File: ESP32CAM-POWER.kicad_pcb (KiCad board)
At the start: 2 copper layers, 80 x 80 mm, 33 parts, among them J1 Screw_Terminal_01x02, J2 Conn_01x03_Male, SW1 TS-1187A-B-A-B, U1 DC-DC-BOARD, U2 ESP32-CAM

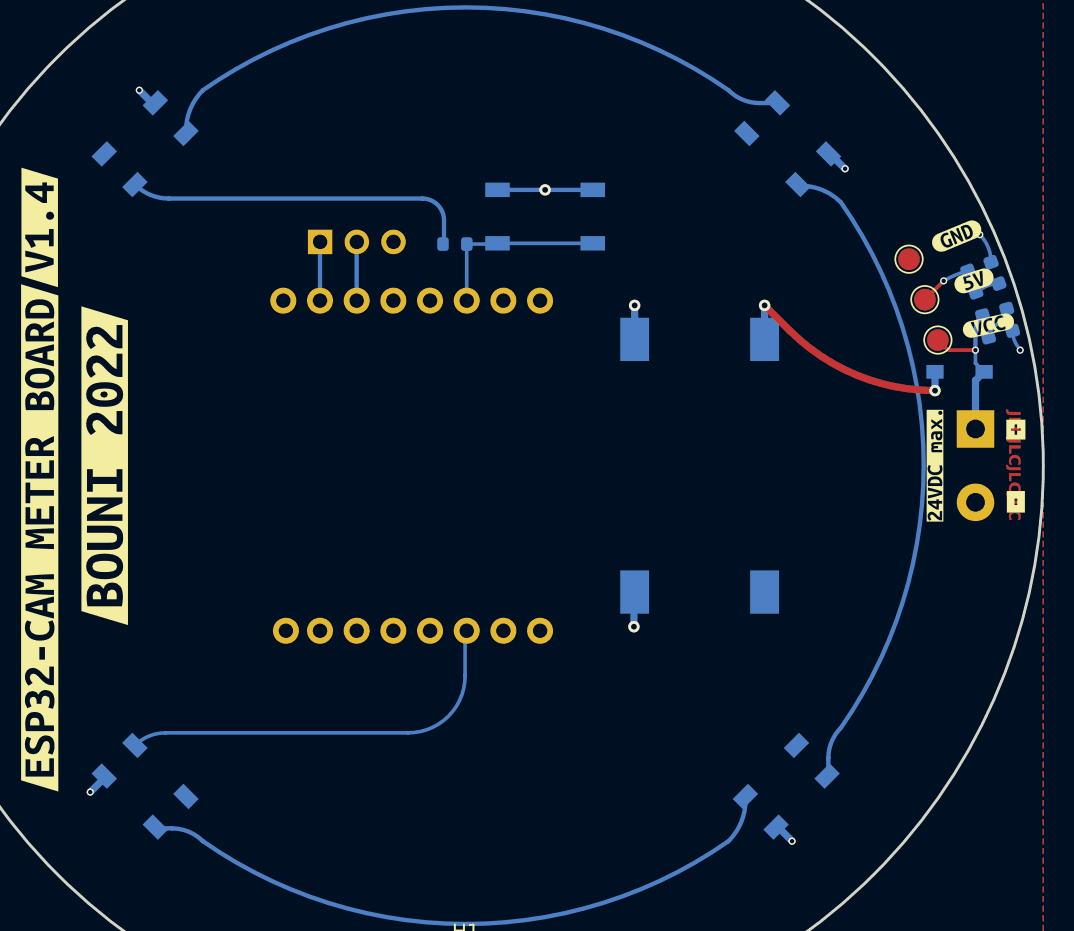
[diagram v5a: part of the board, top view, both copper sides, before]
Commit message: fixed several bugs, replaced DCDC Module with onboard step down
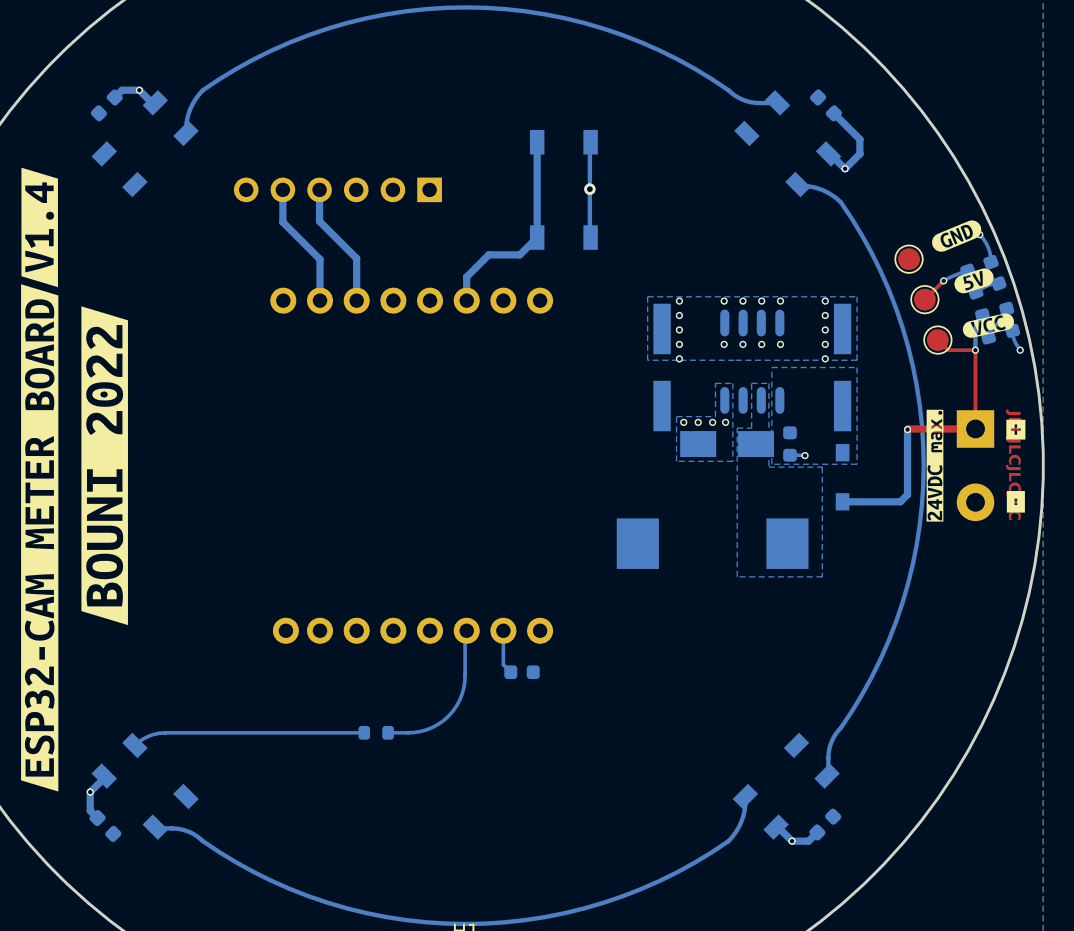
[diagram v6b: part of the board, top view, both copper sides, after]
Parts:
- removed U1: DC-DC-BOARD, bouni:DC-DC-MODULE
- added C1: 0.1uF, Capacitor_SMD:C_0603_1608Metric, B.Cu at (153.9, 94.3)
- added C2: 0.1uF, Capacitor_SMD:C_0603_1608Metric, B.Cu at (125.0, 105.0)
- added C3: 0.1uF, Capacitor_SMD:C_0603_1608Metric, B.Cu at (174.9, 104.8)
- added C4: 0.1uF, Capacitor_SMD:C_0603_1608Metric, B.Cu at (174.9, 55.0)
- added C5: 0.1uF, Capacitor_SMD:C_0603_1608Metric, B.Cu at (125.2, 55.0)
- added C6: 100uF/35V, LCSC:CAP-SMD_BD6.3-L6.6-W6.6-LS7.6-FD, B.Cu at (163.6, 73.2)
- added C7: 0.1uF, Capacitor_SMD:C_0603_1608Metric, B.Cu at (172.5, 78.5)
- added C9: 100uF/35V, LCSC:CAP-SMD_BD6.3-L6.6-W6.6-LS7.6-FD, B.Cu at (176.1, 73.2)
- added D4: SS54, Diode_SMD:D_SMA, B.Cu at (168.1, 78.5)
- added L1: 68uH / 2A, LCSC:IND-SMD_L11.5-W10.0_SMMS1040, B.Cu at (167.1, 85.4)
- added U3: XL1509-5.0E1, LCSC:SOP-8_L4.9-W3.9-P1.27-LS6.0-BL, B.Cu at (169.8, 72.8)
- added kibuzzard-62B5A597: G***, kibuzzard-62B5A597, B.Cu at (142.4, 57.4)
- added kibuzzard-62B5A6D7: G***, kibuzzard-62B5A6D7, B.Cu at (147.5, 63.9)
- added kibuzzard-62B5A6E6: G***, kibuzzard-62B5A6E6, B.Cu at (145.0, 63.9)
- added kibuzzard-62B5A6F5: G***, kibuzzard-62B5A6F5, B.Cu at (142.4, 63.9)
- added kibuzzard-62B5A702: G***, kibuzzard-62B5A702, B.Cu at (139.9, 63.9)
- added kibuzzard-62B5A718: G***, kibuzzard-62B5A718, B.Cu at (137.4, 63.9)
- added kibuzzard-62B5A722: G***, kibuzzard-62B5A722, B.Cu at (134.8, 63.9)
- added kibuzzard-62B5A742: G***, kibuzzard-62B5A742, B.Cu at (145.0, 57.4)
- added kibuzzard-62B5A752: G***, kibuzzard-62B5A752, B.Cu at (134.8, 57.4)
- J2: value Conn_01x03_Male -> Conn_01x06_Male; footprint Connector_PinHeader_2.54mm:PinHeader_1x03_P2.54mm_Vertical -> Connector_PinHeader_2.54mm:PinHeader_1x06_P2.54mm_Vertical
- R3: value 10k -> 470
- moved R3 34.3 mm to (143.8, 98.5), turned to 180 degrees
- moved D3 10.9 mm to (176.1, 80.8), turned to -90 degrees
- moved J2 8.39 mm to (147.5, 60.9), turned to 90 degrees
- moved kibuzzard-62977004 6.02 mm to (137.3, 57.4)
- moved kibuzzard-61C9B205 4.11 mm to (156.8, 55.6), turned to 0 degrees
- moved kibuzzard-62976FF9 4.06 mm to (147.5, 57.4)
- moved kibuzzard-62977011 3.20 mm to (139.9, 57.4)
- moved SW1 2.26 mm to (156.8, 60.9), turned to 90 degrees
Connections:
- J2 pad 1: TX -> GND
- J2 pad 2: RX -> unconnected-(J2-Pin_2)
- J2 pad 3: GND -> +5V
- LED1 pad 3: LED -> Net-(LED1-DI)
- R3 pad 1: +5V -> LED
- R3 pad 2: BOOT -> Net-(LED1-DI)
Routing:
- net +5V: track 27.7 -> 3.63 mm
- net LED: track 28.3 -> 10.6 mm
- net Net-(D3-K): track 17.2 -> 0.00 mm, vias 2 -> 0
- net Net-(LED1-DI): track 0.00 -> 16.1 mm
- net VCC: track 11.4 -> 24.8 mm, vias 1 -> 2
- net GND: track 20.3 -> 30.6 mm, vias 9 -> 30
- net TX: track 4.07 -> 8.73 mm
- net RX: track 4.07 -> 8.73 mm
- net BOOT: track 12.7 -> 14.3 mm
- added copper zone on B.Cu, net GND
- added copper zone on B.Cu, net Net-(D3-K)
- added copper zone on B.Cu, net OUT

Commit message: last cleanups
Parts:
- removed kibuzzard-62976962: G***, kibuzzard-62976962
- removed kibuzzard-6297697D: G***, kibuzzard-6297697D
- removed kibuzzard-629769A0: G***, kibuzzard-629769A0
- removed kibuzzard-629893A5: G***, kibuzzard-629893A5
- added kibuzzard-62B5BECB: G***, kibuzzard-62B5BECB, F.Cu at (120.5, 63.4)
- added kibuzzard-62B5C3E7: G***, kibuzzard-62B5C3E7, F.Cu at (188.4, 77.5)
- added kibuzzard-62B5C3FB: G***, kibuzzard-62B5C3FB, F.Cu at (188.4, 82.5)
- added kibuzzard-62B5C445: G***, kibuzzard-62B5C445, F.Cu at (181.8, 80.1)
- added kibuzzard-62B5C484: G***, kibuzzard-62B5C484, F.Cu at (179.8, 80.1)
- moved D4 6.14 mm to (173.4, 81.6), turned to -90 degrees
- moved C7 3.61 mm to (175.9, 79.6)
- moved L1 1.62 mm to (166.5, 83.9), turned to 90 degrees
- moved D3 1.61 mm to (177.7, 80.6)
- moved kibuzzard-62B5A6D7 0.60 mm to (147.5, 63.3), turned to -90 degrees
- moved kibuzzard-62B5A6E6 0.60 mm to (145.0, 63.3), turned to -90 degrees
- moved kibuzzard-62B5A6F5 0.60 mm to (142.4, 63.3), turned to -90 degrees
- moved kibuzzard-62B5A702 0.60 mm to (139.9, 63.3), turned to -90 degrees
- moved kibuzzard-62B5A718 0.60 mm to (137.4, 63.3), turned to -90 degrees
- moved kibuzzard-62B5A722 0.60 mm to (134.8, 63.3), turned to -90 degrees
- turned kibuzzard-62B5A742 to -90 degrees
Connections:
- net Net-(D3-K) renamed /VIN
- net OUT renamed /OUT
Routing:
- net +5V: track 3.63 -> 24.9 mm, vias 1 -> 3
- net GND: track 30.6 -> 41.3 mm, vias 30 -> 44
- net VCC: track 24.8 -> 22.4 mm
- net BOOT: track 14.3 -> 14.9 mm

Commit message: Ooctober 2024 Update
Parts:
- removed C9: 100uF/35V, LCSC:CAP-SMD_BD6.3-L6.6-W6.6-LS7.6-FD
- removed D4: SS54, Diode_SMD:D_SMA
- removed L1: 68uH / 2A, LCSC:IND-SMD_L11.5-W10.0_SMMS1040
- removed U3: XL1509-5.0E1, LCSC:SOP-8_L4.9-W3.9-P1.27-LS6.0-BL
- removed kibuzzard-611BC015: G***, kibuzzard-611BC015
- removed kibuzzard-61C9B205: G***, kibuzzard-61C9B205
- removed kibuzzard-61CABD37: G***, kibuzzard-61CABD37
- removed kibuzzard-61CABD72: G***, kibuzzard-61CABD72
- removed kibuzzard-62976FF9: G***, kibuzzard-62976FF9
- removed kibuzzard-62977004: G***, kibuzzard-62977004
- removed kibuzzard-62977011: G***, kibuzzard-62977011
- removed kibuzzard-62989351: G***, kibuzzard-62989351
- removed kibuzzard-6298938A: G***, kibuzzard-6298938A
- removed kibuzzard-62B5A597: G***, kibuzzard-62B5A597
- removed kibuzzard-62B5A6D7: G***, kibuzzard-62B5A6D7
- removed kibuzzard-62B5A6E6: G***, kibuzzard-62B5A6E6
- removed kibuzzard-62B5A6F5: G***, kibuzzard-62B5A6F5
- removed kibuzzard-62B5A702: G***, kibuzzard-62B5A702
- removed kibuzzard-62B5A718: G***, kibuzzard-62B5A718
- removed kibuzzard-62B5A722: G***, kibuzzard-62B5A722
- removed kibuzzard-62B5A742: G***, kibuzzard-62B5A742
- removed kibuzzard-62B5A752: G***, kibuzzard-62B5A752
- removed kibuzzard-62B5BECB: G***, kibuzzard-62B5BECB
- removed kibuzzard-62B5C3E7: G***, kibuzzard-62B5C3E7
- removed kibuzzard-62B5C3FB: G***, kibuzzard-62B5C3FB
- removed kibuzzard-62B5C445: G***, kibuzzard-62B5C445
- removed kibuzzard-62B5C484: G***, kibuzzard-62B5C484
- added PS1: TSR_1-2450SM, TRACO-TSR1:TSR124120SM, B.Cu at (169.0, 80.0)
- added R4: 5K1, Resistor_SMD:R_0603_1608Metric, B.Cu at (184.2, 91.5)
- added R5: 5K1, Resistor_SMD:R_0603_1608Metric, B.Cu at (182.4, 96.0)
- added SW2: SW_Omron_B3S, Button_Switch_SMD:SW_SPST_B3S-1000, F.Cu at (139.8, 61.8)
- added TH: ToolingHole, JLCPCB:ToolingHole, F.Cu at (146.0, 37.0)
- added TH: ToolingHole, JLCPCB:ToolingHole, F.Cu at (107.0, 80.0)
- added TH: ToolingHole, JLCPCB:ToolingHole, F.Cu at (154.0, 123.0)
- added U1: CH340X, Package_SO:MSOP-10_3x3mm_P0.5mm, B.Cu at (169.8, 92.5)
- added kibuzzard-66C75903: G***, kibuzzard-66C75903, F.Cu at (153.0, 55.5)
- added kibuzzard-66C7590B: G***, kibuzzard-66C7590B, F.Cu at (139.8, 55.5)
- added kibuzzard-66C81FD1: G***, kibuzzard-66C81FD1, F.Cu at (121.0, 80.0)
- added kibuzzard-66C81FE3: G***, kibuzzard-66C81FE3, F.Cu at (125.0, 80.0)
- added kibuzzard-66C82011: G***, kibuzzard-66C82011, F.Cu at (194.0, 77.5)
- added kibuzzard-66C8202D: G***, kibuzzard-66C8202D, F.Cu at (194.0, 81.0)
- added kibuzzard-66CDCC8A: G***, kibuzzard-66CDCC8A, F.Cu at (169.0, 83.6)
- added kibuzzard-66CDCC90: G***, kibuzzard-66CDCC90, F.Cu at (169.0, 79.2)
- added kibuzzard-66CDCC95: G***, kibuzzard-66CDCC95, F.Cu at (169.0, 75.0)
- C1, C2, C3, C4, C5: footprint Capacitor_SMD:C_0603_1608Metric -> Capacitor_SMD:C_0402_1005Metric
- C6: value 100uF/35V -> 0.1uF; footprint LCSC:CAP-SMD_BD6.3-L6.6-W6.6-LS7.6-FD -> Capacitor_SMD:C_0402_1005Metric
- C7: value 0.1uF -> 100uF; footprint Capacitor_SMD:C_0603_1608Metric -> Capacitor_SMD:CP_Elec_6.3x5.8
- D1: value LED_Y -> LED_B
- D3: value D_Schottky -> 1N5819WS; footprint LCSC:SOD-123_L2.7-W1.6-LS3.7-RD-1 -> Diode_SMD:D_SOD-323
- J1: footprint TerminalBlock_Phoenix:TerminalBlock_Phoenix_MKDS-1,5-2-5.08_1x02_P5.08mm_Horizontal -> SPTAF1:1861933
- J2: value Conn_01x06_Male -> USB_C_Receptacle_USB2.0_16P; footprint Connector_PinHeader_2.54mm:PinHeader_1x06_P2.54mm_Vertical -> LCSC:USB-C-SMD_TYPE-C-6PIN-2MD-073
- LED1, LED2, LED3, LED4: value XL-5050RGBC-WS2812B -> XL-1010RGBC-WS2812B; footprint LCSC:LED-SMD_4P-L5.0-W5.0-BL_XL-5050RGBC -> LCSC:LED-SMD_4P-L1.0-W1.0-TL_XL-1010RGBC-WS2812B
- SW1: value TS-1187A-B-A-B -> SW_Omron_B3S; footprint LCSC:SW-SMD_4P-L5.1-W5.1-P3.70-LS6.5-TL-2 -> Button_Switch_SMD:SW_SPST_B3S-1000; moved to F.Cu
- moved J2 52.5 mm to (187.1, 95.3), turned to -112.5 degrees
- moved C6 17.9 mm to (169.8, 90.0), turned to 180 degrees
- moved TP3 16.8 mm to (171.2, 83.6)
- moved TP2 15.1 mm to (171.2, 79.2)
- moved D3 14.8 mm to (179.6, 95.3), turned to 0 degrees
- moved C7 13.4 mm to (168.6, 68.4), turned to 0 degrees
- moved TP1 13.3 mm to (171.2, 75.0)
- moved J1 6.50 mm to (191.8, 77.5)
- moved D1 5.01 mm to (192.4, 68.3)
- moved D2 5.01 mm to (191.4, 65.1)
- moved R2 5.01 mm to (189.8, 65.7)
- moved R1 5.01 mm to (190.8, 68.8)
- moved H1 4.00 mm to (150.0, 120.0)
- moved H2 4.00 mm to (150.0, 40.0)
- moved SW1 3.89 mm to (153.0, 61.8), turned to -90 degrees
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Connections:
- C6 pad 1: +5V -> GND
- C6 pad 2: GND -> Net-(U1-V3)
- C7 pad 1: /VIN -> +5V
- D3 pad 1: /VIN -> +5V
- D3 pad 2: VCC -> Net-(D3-A)
- LED1 pad 1: +5V -> D1
- LED1 pad 2: Net-(LED1-DO) -> +5V
- LED1 pad 3: Net-(LED1-DI) -> GND
- LED1 pad 4: GND -> Net-(LED1-DIN)
- LED2 pad 1: +5V -> D2
- LED2 pad 2: Net-(LED2-DO) -> +5V
- LED2 pad 3: Net-(LED1-DO) -> GND
- LED2 pad 4: GND -> D1
- LED3 pad 1: +5V -> D3
- LED3 pad 2: Net-(LED3-DO) -> +5V
- LED3 pad 3: Net-(LED2-DO) -> GND
- LED3 pad 4: GND -> D2
- LED4 pad 1: +5V -> unconnected-(LED4-DOUT-Pad1)
- LED4 pad 2: unconnected-(LED4-DO) -> +5V
- LED4 pad 3: Net-(LED3-DO) -> GND
- LED4 pad 4: GND -> D3
- R3 pad 2: Net-(LED1-DI) -> Net-(LED1-DIN)
- SW1 pad 2: GND -> BOOT
- U2 pad 14: RX -> TXD
- U2 pad 15: TX -> RXD
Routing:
- net RXD: track 0.00 -> 52.1 mm, vias 0 -> 2
- net TXD: track 0.00 -> 49.1 mm, vias 0 -> 2
- net Net-(LED1-DO): track 45.3 -> 0.00 mm
- net Net-(LED3-DO): track 45.3 -> 0.00 mm
- net Net-(LED2-DO): track 44.9 -> 0.00 mm
- net VCC: track 22.4 -> 48.3 mm, vias 2 -> 1
- net /D-: track 0.00 -> 17.7 mm
- net +5V: track 24.9 -> 7.41 mm, vias 3 -> 1
- net /D+: track 0.00 -> 17.1 mm, vias 0 -> 2
- net unconnected-(J2-SHIELD-PadS1): track 0.00 -> 17.1 mm
- net Net-(LED1-DIN): track 0.00 -> 16.7 mm
- net Net-(LED1-DI): track 16.1 -> 0.00 mm
- net Net-(D3-A): track 0.00 -> 15.8 mm
- net GND: track 41.3 -> 25.9 mm, vias 44 -> 13
- net RESET: track 0.00 -> 11.3 mm
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- removed copper zone on B.Cu, net /OUT
- removed copper zone on B.Cu, net /VIN
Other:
- board size 80 x 80 mm -> 90 x 90 mm
